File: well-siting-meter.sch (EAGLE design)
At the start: 55 parts, among them IC1 LM336LP, J2 7805, K1 OJE-SH-105HM,000, T1 MOSFET-NCHANNELFQP30N06L, U1 LCD-16X2NOHOLES, U2 ARDUINO_PRO_MINI, U3 EC2, U4 EC2, U5 AD623, U6 AD629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

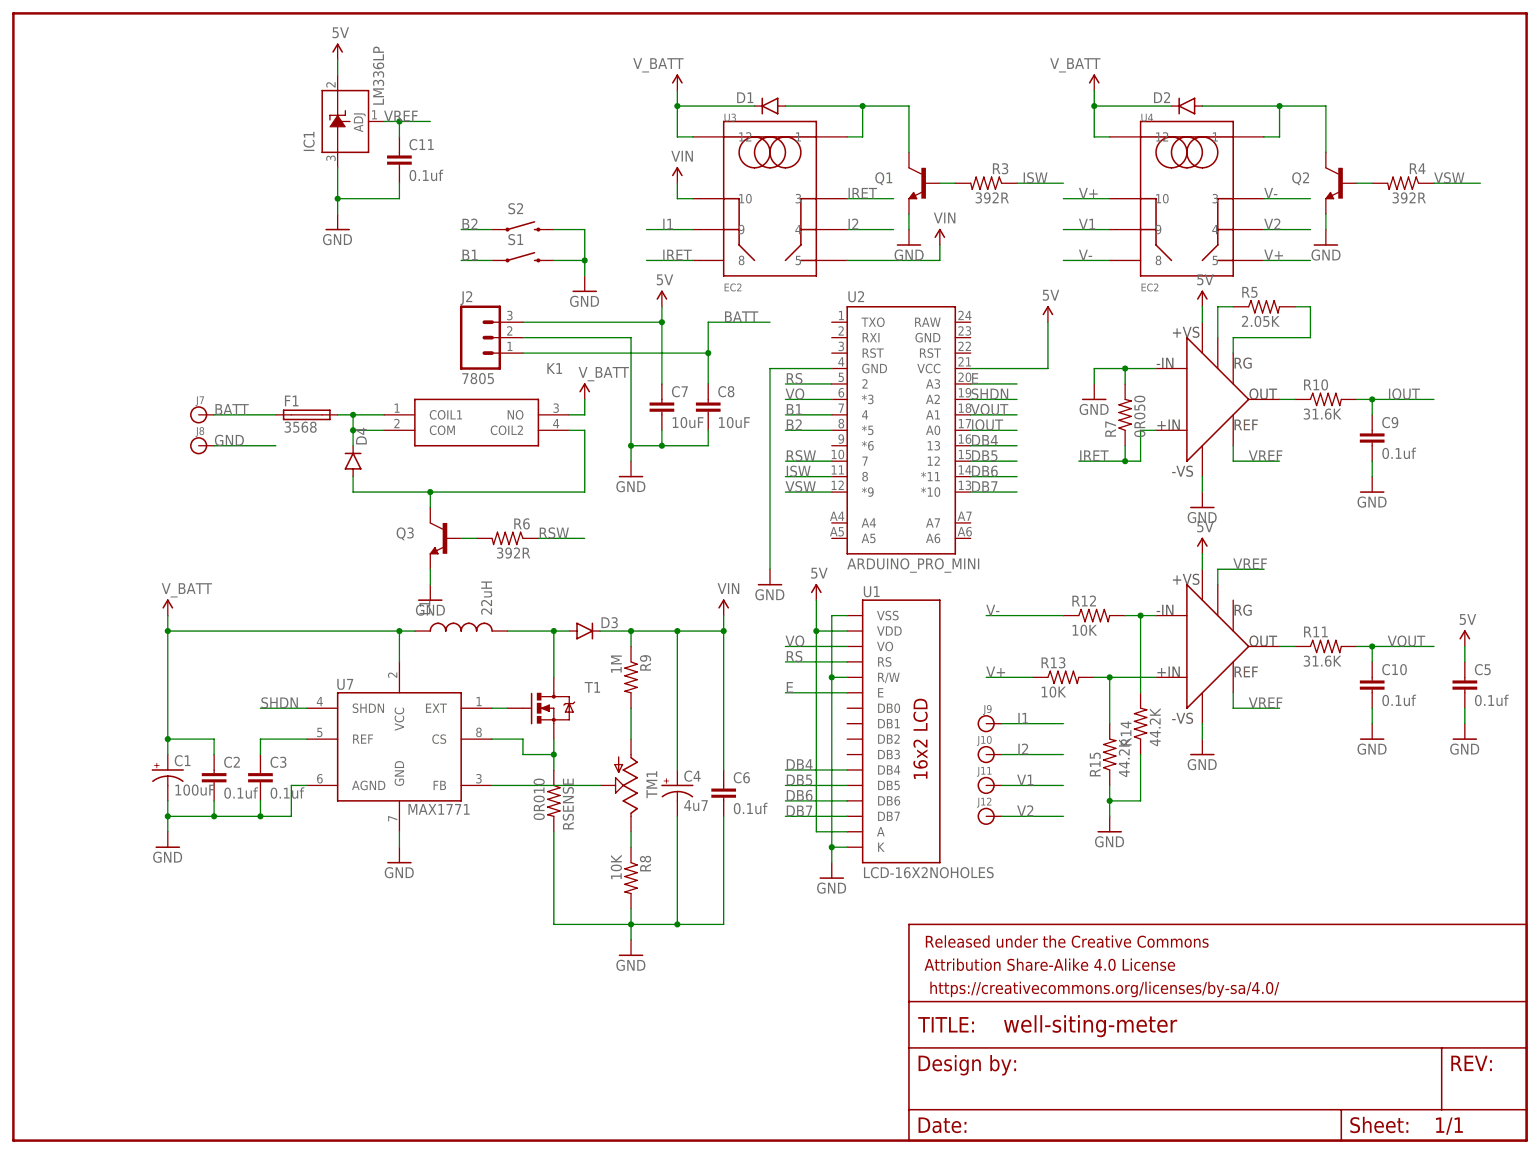
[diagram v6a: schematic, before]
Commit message: rev C initial commit, modifying vref and voltage input resistors
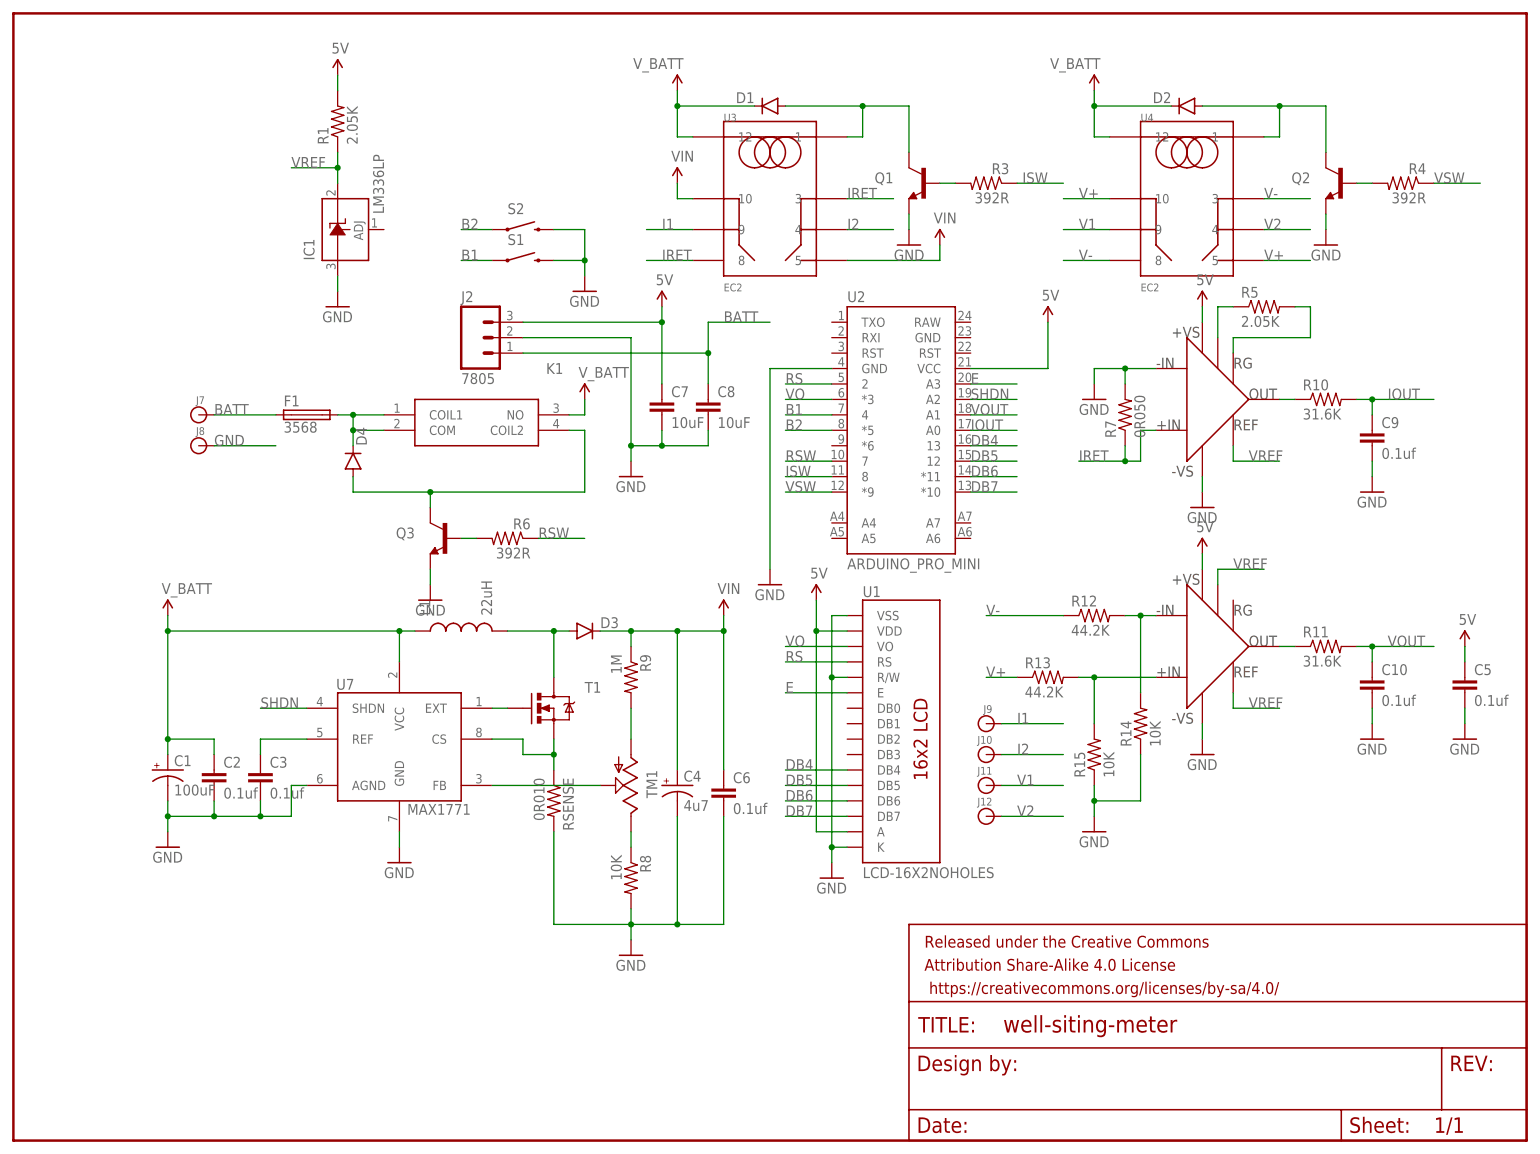
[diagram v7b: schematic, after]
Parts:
- removed C11: 0.1uf, SparkFun-Passives:CAPPTH1
- added R1: 2.05K, SparkFun-Passives:RESISTORPTH-1/4W
- R12, R13: value 10K -> 44.2K; PN 10.0KXBK-ND -> 44.2KXBK-ND
- R14, R15: value 44.2K -> 10K; PN 44.2KXBK-ND -> 10.0KXBK-ND
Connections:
- net 5V: now also R1.2; no longer IC1.C
- net GND: no longer C11.2
- net VREF: now also IC1.C, R1.1; no longer C11.1, IC1.ADJ
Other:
- moved on the sheet: IC1, R13, R15
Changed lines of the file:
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@@
 <?xml version="1.0" encoding="utf-8"?>
 <!DOCTYPE eagle SYSTEM "eagle.dtd">
-<eagle version="9.0.0">
+<eagle version="9.1.0">
 <drawing>
 <settings>
@@
 <attribute name="PN" value="PB876-ND"/>
 </part>
-<part name="R12" library="SparkFun-Passives" deviceset="RESISTOR" device="PTH-1/4W" value="10K">
+<part name="R12" library="SparkFun-Passives" deviceset="RESISTOR" device="PTH-1/4W" value="44.2K">
+<attribute name="PN" value="44.2KXBK-ND"/>
+</part>
+<part name="R13" library="SparkFun-Passives" deviceset="RESISTOR" device="PTH-1/4W" value="44.2K">
+<attribute name="PN" value="44.2KXBK-ND"/>
+</part>
+<part name="R14" library="SparkFun-Passives" deviceset="RESISTOR" device="PTH-1/4W" value="10K">
 <attribute name="PN" value="10.0KXBK-ND"/>
 </part>
-<part name="R13" library="SparkFun-Passives" deviceset="RESISTOR" device="PTH-1/4W" value="10K">
+<part name="R15" library="SparkFun-Passives" deviceset="RESISTOR" device="PTH-1/4W" value="10K">
 <attribute name="PN" value="10.0KXBK-ND"/>
-</part>
-<part name="R14" library="SparkFun-Passives" deviceset="RESISTOR" device="PTH-1/4W" value="44.2K">
-<attribute name="PN" value="44.2KXBK-ND"/>
-</part>
-<part name="R15" library="SparkFun-Passives" deviceset="RESISTOR" device="PTH-1/4W" value="44.2K">
-<attribute name="PN" value="44.2KXBK-ND"/>
 </part>
 <part name="GND17" library="SparkFun-Aesthetics" deviceset="GND" device=""/>
@@
 </part>
 <part name="SUPPLY14" library="SparkFun-Aesthetics" deviceset="5V" device=""/>
-<part name="C11" library="SparkFun-Passives" deviceset="CAP" device="PTH1" value="0.1uf">
-<attribute name="PN" value="BC2665CT-ND"/>
+<part name="R1" library="SparkFun-Passives" deviceset="RESISTOR" device="PTH-1/4W" value="2.05K">
+<attribute name="PN" value="2.05KXBK-ND"/>
 </part>
 </parts>
@@
 </instance>
 <instance part="SUPPLY2" gate="G$1" x="170.18" y="134.62"/>
-<instance part="GND2" gate="1" x="53.34" y="149.86"/>
+<instance part="GND2" gate="1" x="53.34" y="137.16"/>
 <instance part="GND3" gate="1" x="147.32" y="147.32" rot="MR0"/>
 <instance part="GND4" gate="1" x="215.9" y="147.32" rot="MR0"/>
@@
 <attribute name="PN" x="177.8" y="86.36" size="1.778" layer="96" display="off"/>
 </instance>
-<instance part="R13" gate="G$1" x="172.72" y="76.2">
-<attribute name="PN" x="172.72" y="76.2" size="1.778" layer="96" display="off"/>
+<instance part="R13" gate="G$1" x="170.18" y="76.2">
+<attribute name="PN" x="170.18" y="76.2" size="1.778" layer="96" display="off"/>
 </instance>
 <instance part="R14" gate="G$1" x="185.42" y="68.58" rot="R90">
 <attribute name="PN" x="185.42" y="68.58" size="1.778" layer="96" rot="R90" display="off"/>
 </instance>
-<instance part="R15" gate="G$1" x="180.34" y="63.5" rot="R90">
-<attribute name="PN" x="180.34" y="63.5" size="1.778" layer="96" rot="R90" display="off"/>
-</instance>
-<instance part="GND17" gate="1" x="180.34" y="50.8"/>
+<instance part="R15" gate="G$1" x="177.8" y="63.5" rot="R90">
+<attribute name="PN" x="177.8" y="63.5" size="1.778" layer="96" rot="R90" display="off"/>
+</instance>
+<instance part="GND17" gate="1" x="177.8" y="50.8"/>
 <instance part="C5" gate="G$1" x="238.76" y="73.66">
 <attribute name="PN" x="238.76" y="73.66" size="1.778" layer="96" display="off"/>
@@
 <instance part="SUPPLY12" gate="G$1" x="238.76" y="81.28"/>
 <instance part="GND18" gate="1" x="238.76" y="66.04"/>
-<instance part="IC1" gate="G$1" x="53.34" y="167.64" rot="R90">
+<instance part="IC1" gate="G$1" x="53.34" y="149.86" rot="R90">
+<attribute name="PN" x="53.34" y="149.86" size="1.778" layer="96" rot="R90" display="off"/>
+</instance>
+<instance part="SUPPLY14" gate="G$1" x="53.34" y="175.26"/>
+<instance part="R1" gate="G$1" x="53.34" y="167.64" rot="R90">
 <attribute name="PN" x="53.34" y="167.64" size="1.778" layer="96" rot="R90" display="off"/>
-</instance>
-<instance part="SUPPLY14" gate="G$1" x="53.34" y="177.8"/>
-<instance part="C11" gate="G$1" x="63.5" y="160.02">
-<attribute name="PN" x="63.5" y="160.02" size="1.778" layer="96" display="off"/>
 </instance>
 </instances>
@@
 <pinref part="R15" gate="G$1" pin="1"/>
 <pinref part="GND17" gate="1" pin="GND"/>
-<wire x1="180.34" y1="58.42" x2="180.34" y2="55.88" width="0.1524" layer="91"/>
-<junction x="180.34" y="55.88"/>
-<wire x1="180.34" y1="55.88" x2="180.34" y2="53.34" width="0.1524" layer="91"/>
+<wire x1="177.8" y1="58.42" x2="177.8" y2="55.88" width="0.1524" layer="91"/>
+<junction x="177.8" y="55.88"/>
+<wire x1="177.8" y1="55.88" x2="177.8" y2="53.34" width="0.1524" layer="91"/>
 <pinref part="R14" gate="G$1" pin="1"/>
 <wire x1="185.42" y1="63.5" x2="185.42" y2="55.88" width="0.1524" layer="91"/>
-<wire x1="185.42" y1="55.88" x2="180.34" y2="55.88" width="0.1524" layer="91"/>
+<wire x1="185.42" y1="55.88" x2="177.8" y2="55.88" width="0.1524" layer="91"/>
 </segment>
 <segment>
@@
 <pinref part="IC1" gate="G$1" pin="A"/>
 <pinref part="GND2" gate="1" pin="GND"/>
-<wire x1="53.34" y1="160.02" x2="53.34" y2="154.94" width="0.1524" layer="91"/>
-<junction x="53.34" y="154.94"/>
-<wire x1="53.34" y1="154.94" x2="53.34" y2="152.4" width="0.1524" layer="91"/>
-<pinref part="C11" gate="G$1" pin="2"/>
-<wire x1="53.34" y1="154.94" x2="63.5" y2="154.94" width="0.1524" layer="91"/>
-<wire x1="63.5" y1="154.94" x2="63.5" y2="157.48" width="0.1524" layer="91"/>
+<wire x1="53.34" y1="142.24" x2="53.34" y2="139.7" width="0.1524" layer="91"/>
 </segment>
 </net>
@@
 <segment>
 <pinref part="SUPPLY14" gate="G$1" pin="5V"/>
-<pinref part="IC1" gate="G$1" pin="C"/>
-<wire x1="53.34" y1="177.8" x2="53.34" y2="175.26" width="0.1524" layer="91"/>
+<pinref part="R1" gate="G$1" pin="2"/>
+<wire x1="53.34" y1="175.26" x2="53.34" y2="172.72" width="0.1524" layer="91"/>
 </segment>
 </net>
@@
 <segment>
 <pinref part="R13" gate="G$1" pin="1"/>
-<wire x1="167.64" y1="76.2" x2="160.02" y2="76.2" width="0.1524" layer="91"/>
+<wire x1="165.1" y1="76.2" x2="160.02" y2="76.2" width="0.1524" layer="91"/>
 <label x="160.02" y="76.2" size="1.778" layer="95"/>
 </segment>
@@
 <net name="VREF" class="0">
 <segment>
-<label x="60.96" y="167.64" size="1.778" layer="95"/>
-<pinref part="IC1" gate="G$1" pin="ADJ"/>
-<wire x1="60.96" y1="167.64" x2="63.5" y2="167.64" width="0.1524" layer="91"/>
-<junction x="63.5" y="167.64"/>
-<wire x1="63.5" y1="167.64" x2="68.58" y2="167.64" width="0.1524" layer="91"/>
-<pinref part="C11" gate="G$1" pin="1"/>
-<wire x1="63.5" y1="165.1" x2="63.5" y2="167.64" width="0.1524" layer="91"/>
-</segment>
-<segment>
 <pinref part="U5" gate="G$1" pin="REF"/>
 <wire x1="200.66" y1="114.3" x2="200.66" y2="111.76" width="0.1524" layer="91"/>
@@
 <wire x1="198.12" y1="93.98" x2="205.74" y2="93.98" width="0.1524" layer="91"/>
 <label x="200.66" y="93.98" size="1.778" layer="95"/>
+</segment>
+<segment>
+<pinref part="R1" gate="G$1" pin="1"/>
+<pinref part="IC1" gate="G$1" pin="C"/>
+<wire x1="53.34" y1="162.56" x2="53.34" y2="160.02" width="0.1524" layer="91"/>
+<junction x="53.34" y="160.02"/>
+<wire x1="53.34" y1="160.02" x2="53.34" y2="157.48" width="0.1524" layer="91"/>
+<wire x1="53.34" y1="160.02" x2="45.72" y2="160.02" width="0.1524" layer="91"/>
+<label x="45.72" y="160.02" size="1.778" layer="95"/>
 </segment>
 </net>
@@
 <pinref part="R13" gate="G$1" pin="2"/>
 <pinref part="U6" gate="G$1" pin="+IN"/>
-<wire x1="177.8" y1="76.2" x2="180.34" y2="76.2" width="0.1524" layer="91"/>
-<junction x="180.34" y="76.2"/>
-<wire x1="180.34" y1="76.2" x2="187.96" y2="76.2" width="0.1524" layer="91"/>
+<wire x1="175.26" y1="76.2" x2="177.8" y2="76.2" width="0.1524" layer="91"/>
+<junction x="177.8" y="76.2"/>
+<wire x1="177.8" y1="76.2" x2="187.96" y2="76.2" width="0.1524" layer="91"/>
 <pinref part="R15" gate="G$1" pin="2"/>
-<wire x1="180.34" y1="76.2" x2="180.34" y2="68.58" width="0.1524" layer="91"/>
-</segment>
-</net>
+<wire x1="177.8" y1="76.2" x2="177.8" y2="68.58" width="0.1524" layer="91"/>
+</segment>
+</net>
